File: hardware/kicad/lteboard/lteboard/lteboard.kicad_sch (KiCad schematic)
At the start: 0 parts

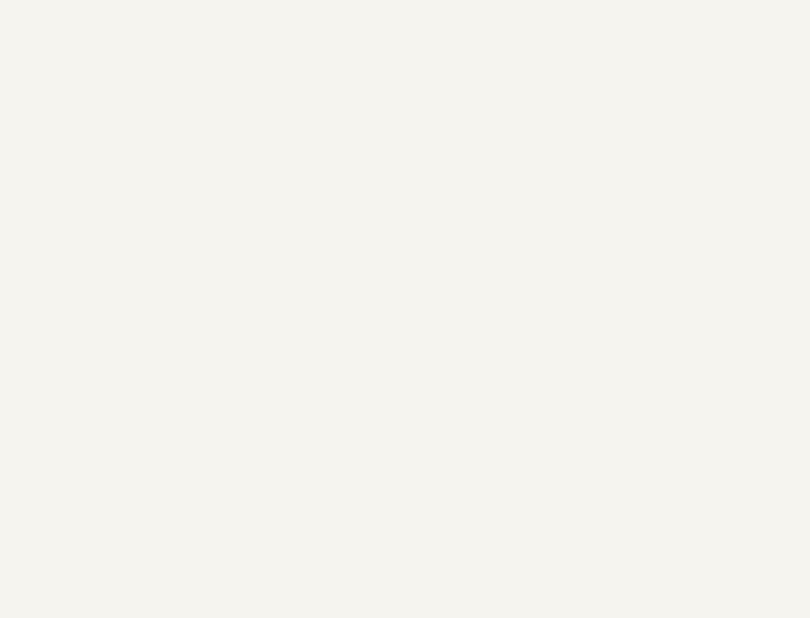
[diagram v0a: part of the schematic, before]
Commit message: Complete Ethernet subsystem: schematic capture done, termination network confirmed via direct datasheet read
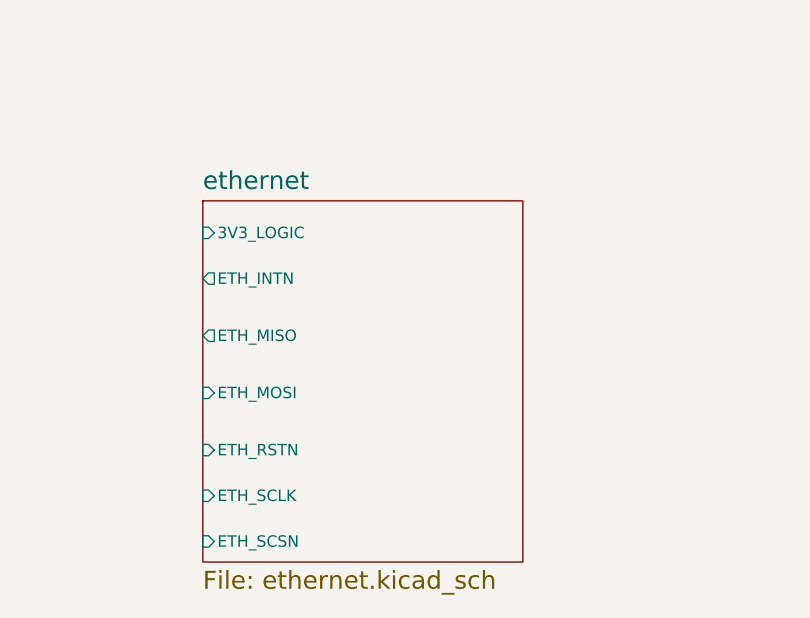
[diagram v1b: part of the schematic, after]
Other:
- added sheet ethernet (ethernet.kicad_sch)
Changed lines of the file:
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@@
+	)
+	(sheet
+		(at 71.12 131.064)
+		(size 35.56 40.132)
+		(exclude_from_sim no)
+		(in_bom yes)
+		(on_board yes)
+		(dnp no)
+		(fields_autoplaced yes)
+		(stroke
+			(width 0.1524)
+			(type solid)
+		)
+		(fill
+			(color 0 0 0 0.0000)
+		)
+		(property "Sheetname" "ethernet"
+			(at 71.12 129.9874 0)
+			(effects
+				(font
+					(size 2 2)
+				)
+				(justify left bottom)
+			)
+		)
+		(property "Sheetfile" "ethernet.kicad_sch"
+			(at 71.12 172.0726 0)
+			(effects
+				(font
+					(size 2 2)
+				)
+				(justify left top)
+			)
+		)
+		(pin "3V3_LOGIC" input
+			(at 71.12 134.62 180)
+			(effects
+				(font
+					(size 1.27 1.27)
+				)
+				(justify left)
+			)
+		)
+		(pin "ETH_INTN" output
+			(at 71.12 139.7 180)
+			(effects
+				(font
+					(size 1.27 1.27)
+				)
+				(justify left)
+			)
+		)
+		(pin "ETH_MISO" output
+			(at 71.12 146.05 180)
+			(effects
+				(font
+					(size 1.27 1.27)
+				)
+				(justify left)
+			)
+		)
+		(pin "ETH_MOSI" input
+			(at 71.12 152.4 180)
+			(effects
+				(font
+					(size 1.27 1.27)
+				)
+				(justify left)
+			)
+		)
+		(pin "ETH_RSTN" input
+			(at 71.12 158.75 180)
+			(effects
+				(font
+					(size 1.27 1.27)
+				)
+				(justify left)
+			)
+		)
+		(pin "ETH_SCLK" input
+			(at 71.12 163.83 180)
+			(effects
+				(font
+					(size 1.27 1.27)
+				)
+				(justify left)
+			)
+		)
+		(pin "ETH_SCSN" input
+			(at 71.12 168.91 180)
+			(effects
+				(font
+					(size 1.27 1.27)
+				)
+				(justify left)
+			)
+		)
+		(instances
+			(project "lteboard"
+				(path "/e3cbe890-827c-4e3e-bf4e-d33595c4d0b3"
+					(page "4")
+				)
+			)
+		)
 	)
 	(sheet
